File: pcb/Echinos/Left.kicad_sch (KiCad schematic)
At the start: 39 parts, among them J1 USB_C_Receptacle_USB2.0, J2 TagConnect_6pins, J206 Conn_01x06_Pin, J208 FPC (PCB), J301 SATA-7p, J4 FPC_VIK, SW1 SW_Push, SW2 SW_Push, U2 W25Q128JVS, U3 ESD7L5.0DT5G-N, U5 XC6210B332MR-G, U7 D3V3F4U6S-7

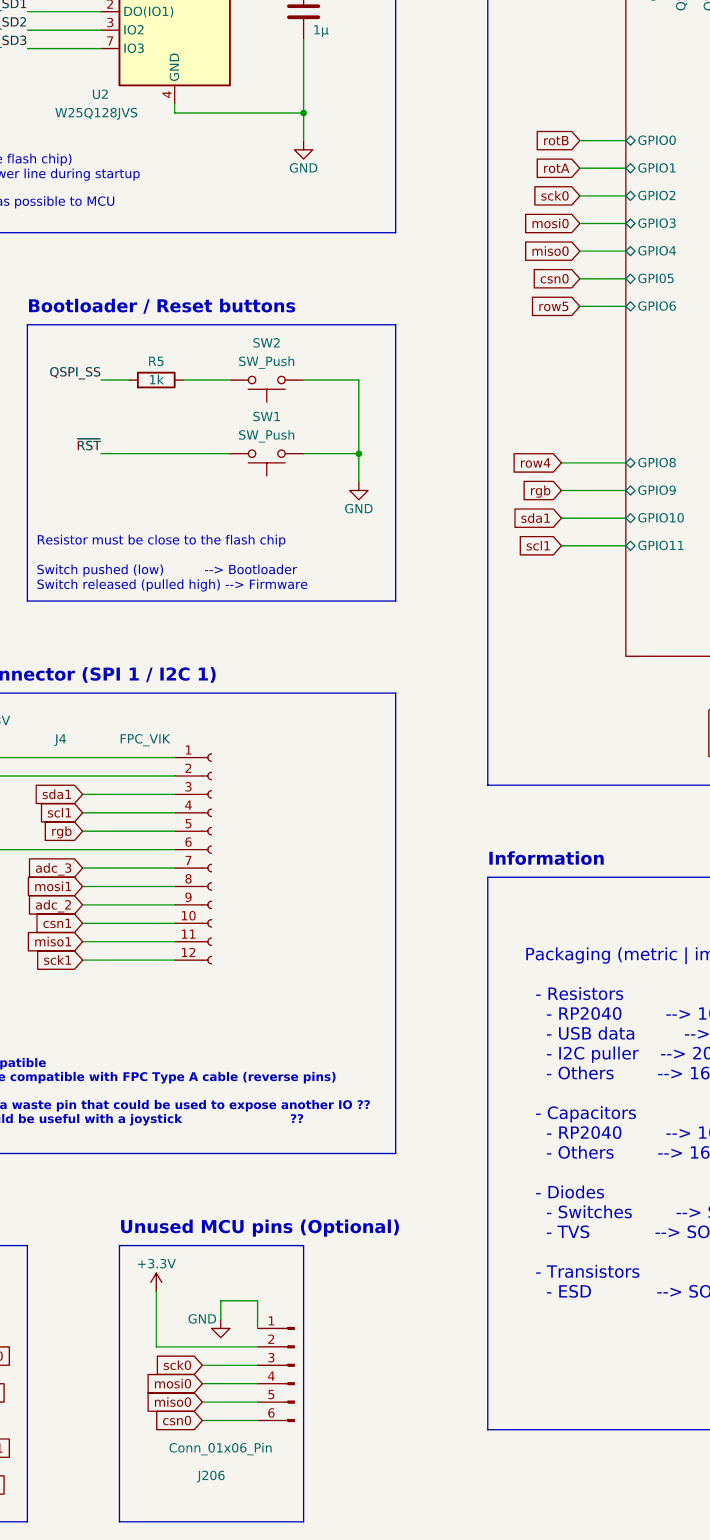
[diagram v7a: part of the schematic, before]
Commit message: ✨ [PCB] - Make some place to add a FPC connector providing a way to expand the matrix / number of keys or add a joystick and I2C pull-up resistors. Improve routing in order to minimize the number of vias.
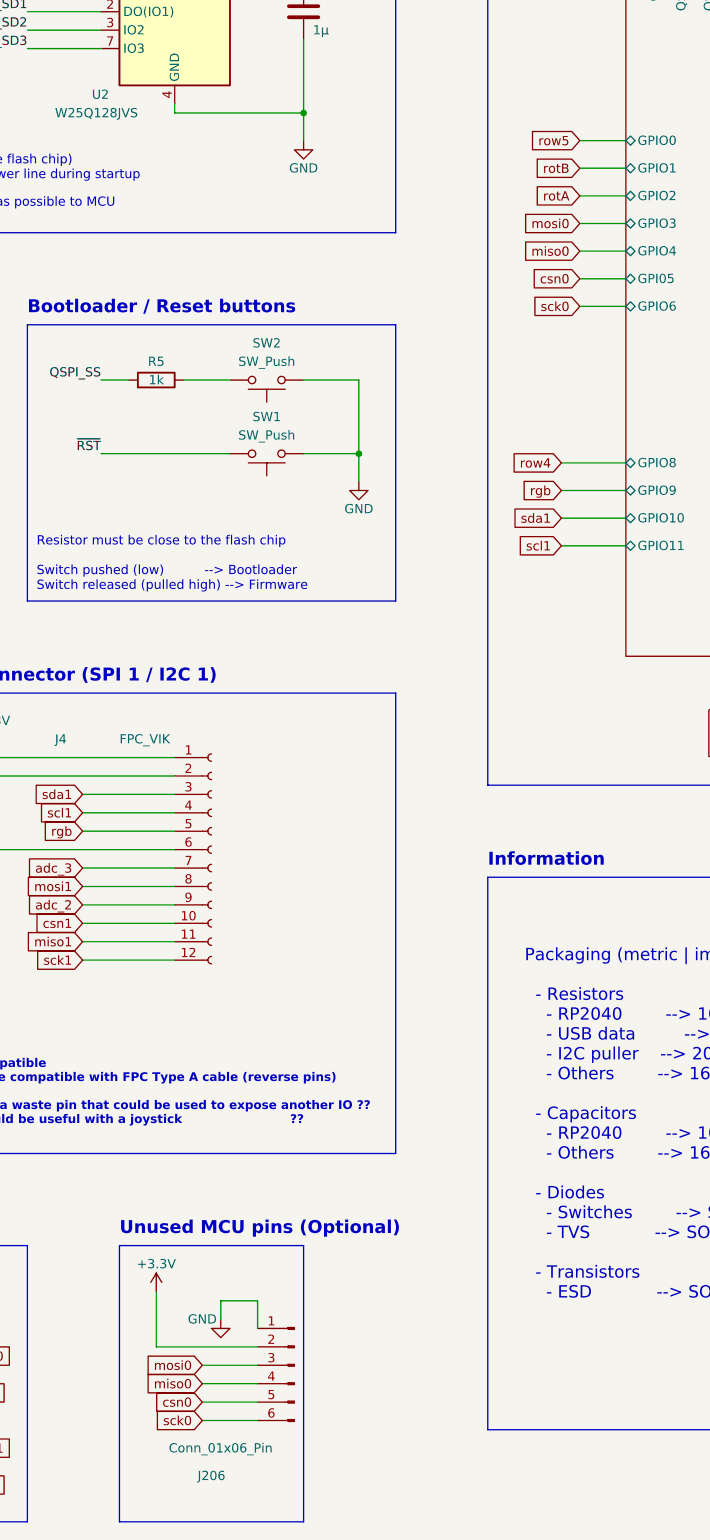
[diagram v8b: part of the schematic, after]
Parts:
- R11, R13: footprint Resistor_SMD:R_0805_2012Metric_Pad1.20x1.40mm_HandSolder -> Resistor_SMD:R_0402_1005Metric_Pad0.72x0.64mm_HandSolder; LCSC C413739 -> (none)
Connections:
- net csn0: now also J206.5 (Pin_5); no longer J206.6 (Pin_6)
- net miso0: now also J206.4 (Pin_4); no longer J206.5 (Pin_5)
- net mosi0: now also J206.3 (Pin_3); no longer J206.4 (Pin_4)
- net sck0: now also J206.6 (Pin_6); no longer J206.3 (Pin_3)
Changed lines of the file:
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@@
-    )
-  )
-  (global_label "mosi0" (shape input) (at 252.73 234.95 180) (fields_autoplaced)
-    (effects (font (size 1.27 1.27)) (justify right))
-    (property "Intersheetrefs" "${INTERSHEET_REFS}" (at 244.1395 234.95 0)
-      (effects (font (size 1.27 1.27)) (justify right) hide)
     )
   )
@@
     )
   )
-  (global_label "sck0" (shape input) (at 252.73 232.41 180) (fields_autoplaced)
-    (effects (font (size 1.27 1.27)) (justify right))
-    (property "Intersheetrefs" "${INTERSHEET_REFS}" (at 245.4699 232.41 0)
-      (effects (font (size 1.27 1.27)) (justify right) hide)
-    )
-  )
   (global_label "col5" (shape input) (at 134.62 163.83 0) (fields_autoplaced)
     (effects (font (size 1.27 1.27)) (justify left))
@@
     )
   )
-  (global_label "rotB" (shape input) (at 304.8 63.5 180) (fields_autoplaced)
-    (effects (font (size 1.27 1.27)) (justify right))
-    (property "Intersheetrefs" "${INTERSHEET_REFS}" (at 297.8839 63.5 0)
-      (effects (font (size 1 1)) (justify right) hide)
-    )
-  )
   (global_label "TX" (shape bidirectional) (at 204.47 106.68 0) (fields_autoplaced)
     (effects (font (size 1.27 1.27)) (justify left))
@@
     )
   )
+  (global_label "rotB" (shape input) (at 304.8 67.31 180) (fields_autoplaced)
+    (effects (font (size 1.27 1.27)) (justify right))
+    (property "Intersheetrefs" "${INTERSHEET_REFS}" (at 297.8839 67.31 0)
+      (effects (font (size 1 1)) (justify right) hide)
+    )
+  )
   (global_label "sda0" (shape input) (at 219.71 231.14 0) (fields_autoplaced)
     (effects (font (size 1.27 1.27)) (justify left))
@@
     )
   )
-  (global_label "csn0" (shape input) (at 252.73 240.03 180) (fields_autoplaced)
-    (effects (font (size 1.27 1.27)) (justify right))
-    (property "Intersheetrefs" "${INTERSHEET_REFS}" (at 245.349 240.03 0)
-      (effects (font (size 1.27 1.27)) (justify right) hide)
-    )
-  )
-  (global_label "row5" (shape input) (at 304.8 86.36 180) (fields_autoplaced)
-    (effects (font (size 1.27 1.27)) (justify right))
-    (property "Intersheetrefs" "${INTERSHEET_REFS}" (at 297.3396 86.36 0)
-      (effects (font (size 1 1)) (justify right) hide)
-    )
-  )
   (global_label "adc_3" (shape input) (at 381 57.15 0) (fields_autoplaced)
     (effects (font (size 1.27 1.27)) (justify left))
@@
     )
   )
-  (global_label "sck0" (shape input) (at 304.8 71.12 180) (fields_autoplaced)
-    (effects (font (size 1.27 1.27)) (justify right))
-    (property "Intersheetrefs" "${INTERSHEET_REFS}" (at 297.5399 71.12 0)
-      (effects (font (size 1.27 1.27)) (justify right) hide)
-    )
-  )
-  (global_label "rotA" (shape input) (at 304.8 67.31 180) (fields_autoplaced)
-    (effects (font (size 1.27 1.27)) (justify right))
-    (property "Intersheetrefs" "${INTERSHEET_REFS}" (at 298.0653 67.31 0)
-      (effects (font (size 1 1)) (justify right) hide)
-    )
-  )
   (global_label "scl1" (shape input) (at 236.22 156.21 180) (fields_autoplaced)
     (effects (font (size 1.27 1.27)) (justify right))
@@
     )
   )
+  (global_label "miso0" (shape input) (at 252.73 234.95 180) (fields_autoplaced)
+    (effects (font (size 1.27 1.27)) (justify right))
+    (property "Intersheetrefs" "${INTERSHEET_REFS}" (at 244.1395 234.95 0)
+      (effects (font (size 1.27 1.27)) (justify right) hide)
+    )
+  )
   (global_label "sda1" (shape input) (at 219.71 243.84 0) (fields_autoplaced)
     (effects (font (size 1.27 1.27)) (justify left))
@@
     )
   )
+  (global_label "sck0" (shape input) (at 252.73 240.03 180) (fields_autoplaced)
+    (effects (font (size 1.27 1.27)) (justify right))
+    (property "Intersheetrefs" "${INTERSHEET_REFS}" (at 245.4699 240.03 0)
+      (effects (font (size 1.27 1.27)) (justify right) hide)
+    )
+  )
   (global_label "col3" (shape output) (at 381 77.47 0) (fields_autoplaced)
     (effects (font (size 1.27 1.27)) (justify left))
@@
     )
   )
+  (global_label "mosi0" (shape input) (at 252.73 232.41 180) (fields_autoplaced)
+    (effects (font (size 1.27 1.27)) (justify right))
+    (property "Intersheetrefs" "${INTERSHEET_REFS}" (at 244.1395 232.41 0)
+      (effects (font (size 1.27 1.27)) (justify right) hide)
+    )
+  )
   (global_label "scl0" (shape input) (at 219.71 236.22 0) (fields_autoplaced)
     (effects (font (size 1.27 1.27)) (justify left))
@@
     )
   )
+  (global_label "sck0" (shape input) (at 304.8 86.36 180) (fields_autoplaced)
+    (effects (font (size 1.27 1.27)) (justify right))
+    (property "Intersheetrefs" "${INTERSHEET_REFS}" (at 297.5399 86.36 0)
+      (effects (font (size 1.27 1.27)) (justify right) hide)
+    )
+  )
   (global_label "sck1" (shape input) (at 236.22 176.53 180) (fields_autoplaced)
     (effects (font (size 1.27 1.27)) (justify right))
@@
     )
   )
-  (global_label "miso0" (shape input) (at 252.73 237.49 180) (fields_autoplaced)
-    (effects (font (size 1.27 1.27)) (justify right))
-    (property "Intersheetrefs" "${INTERSHEET_REFS}" (at 244.1395 237.49 0)
-      (effects (font (size 1.27 1.27)) (justify right) hide)
-    )
-  )
   (global_label "adc_1" (shape output) (at 135.89 166.37 0) (fields_autoplaced)
     (effects (font (size 1.27 1.27)) (justify left))
@@
     )
   )
+  (global_label "row5" (shape input) (at 304.8 63.5 180) (fields_autoplaced)
+    (effects (font (size 1.27 1.27)) (justify right))
+    (property "Intersheetrefs" "${INTERSHEET_REFS}" (at 297.3396 63.5 0)
+      (effects (font (size 1 1)) (justify right) hide)
+    )
+  )
   (global_label "row2" (shape input) (at 381 116.84 0) (fields_autoplaced)
     (effects (font (size 1.27 1.27)) (justify left))
@@
     (property "Intersheetrefs" "${INTERSHEET_REFS}" (at 388.4604 120.65 0)
       (effects (font (size 1 1)) (justify left) hide)
+    )
+  )
+  (global_label "rotA" (shape input) (at 304.8 71.12 180) (fields_autoplaced)
+    (effects (font (size 1.27 1.27)) (justify right))
+    (property "Intersheetrefs" "${INTERSHEET_REFS}" (at 298.0653 71.12 0)
+      (effects (font (size 1 1)) (justify right) hide)
+    )
+  )
+  (global_label "csn0" (shape input) (at 252.73 237.49 180) (fields_autoplaced)
+    (effects (font (size 1.27 1.27)) (justify right))
+    (property "Intersheetrefs" "${INTERSHEET_REFS}" (at 245.349 237.49 0)
+      (effects (font (size 1.27 1.27)) (justify right) hide)
     )
   )
@@
       (effects (font (size 1.27 1.27)))
     )
-    (property "Footprint" "Resistor_SMD:R_0805_2012Metric_Pad1.20x1.40mm_HandSolder" (at 213.36 245.618 90)
+    (property "Footprint" "Resistor_SMD:R_0402_1005Metric_Pad0.72x0.64mm_HandSolder" (at 213.36 245.618 90)
       (effects (font (size 1.27 1.27)) hide)
     )
@@
       (effects (font (size 1.27 1.27)) hide)
     )
-    (property "LCSC" "C413739" (at 213.36 243.84 0)
+    (property "LCSC" "" (at 213.36 243.84 0)
       (effects (font (size 1.27 1.27)) hide)
     )
@@
       (effects (font (size 1.27 1.27)))
     )
-    (property "Footprint" "Resistor_SMD:R_0805_2012Metric_Pad1.20x1.40mm_HandSolder" (at 213.36 250.698 90)
+    (property "Footprint" "Resistor_SMD:R_0402_1005Metric_Pad0.72x0.64mm_HandSolder" (at 213.36 250.698 90)
       (effects (font (size 1.27 1.27)) hide)
     )
@@
       (effects (font (size 1.27 1.27)) hide)
     )
-    (property "LCSC" "C413739" (at 213.36 248.92 0)
-      (effects (font (size 1.27 1.27)) hide)
-    )
+    (property "LCSC" "" (at 213.36 248.92 0)
+      (effects (font (size 1.27 1.27)) hide)
+    )
